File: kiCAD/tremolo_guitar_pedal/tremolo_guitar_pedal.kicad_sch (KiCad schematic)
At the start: 34 parts, among them CN3 NUCLEO-L432KC, CN4 NUCLEO-L432KC, J1 NJ2FD-V, J2 NJ2FD-V, J3 UPduino v3.1, J5 UPduino v3.1, SW1 3PDT Footswitch, U1 NE5532, U2 PCM5102, U3 LD1117DT33CTR

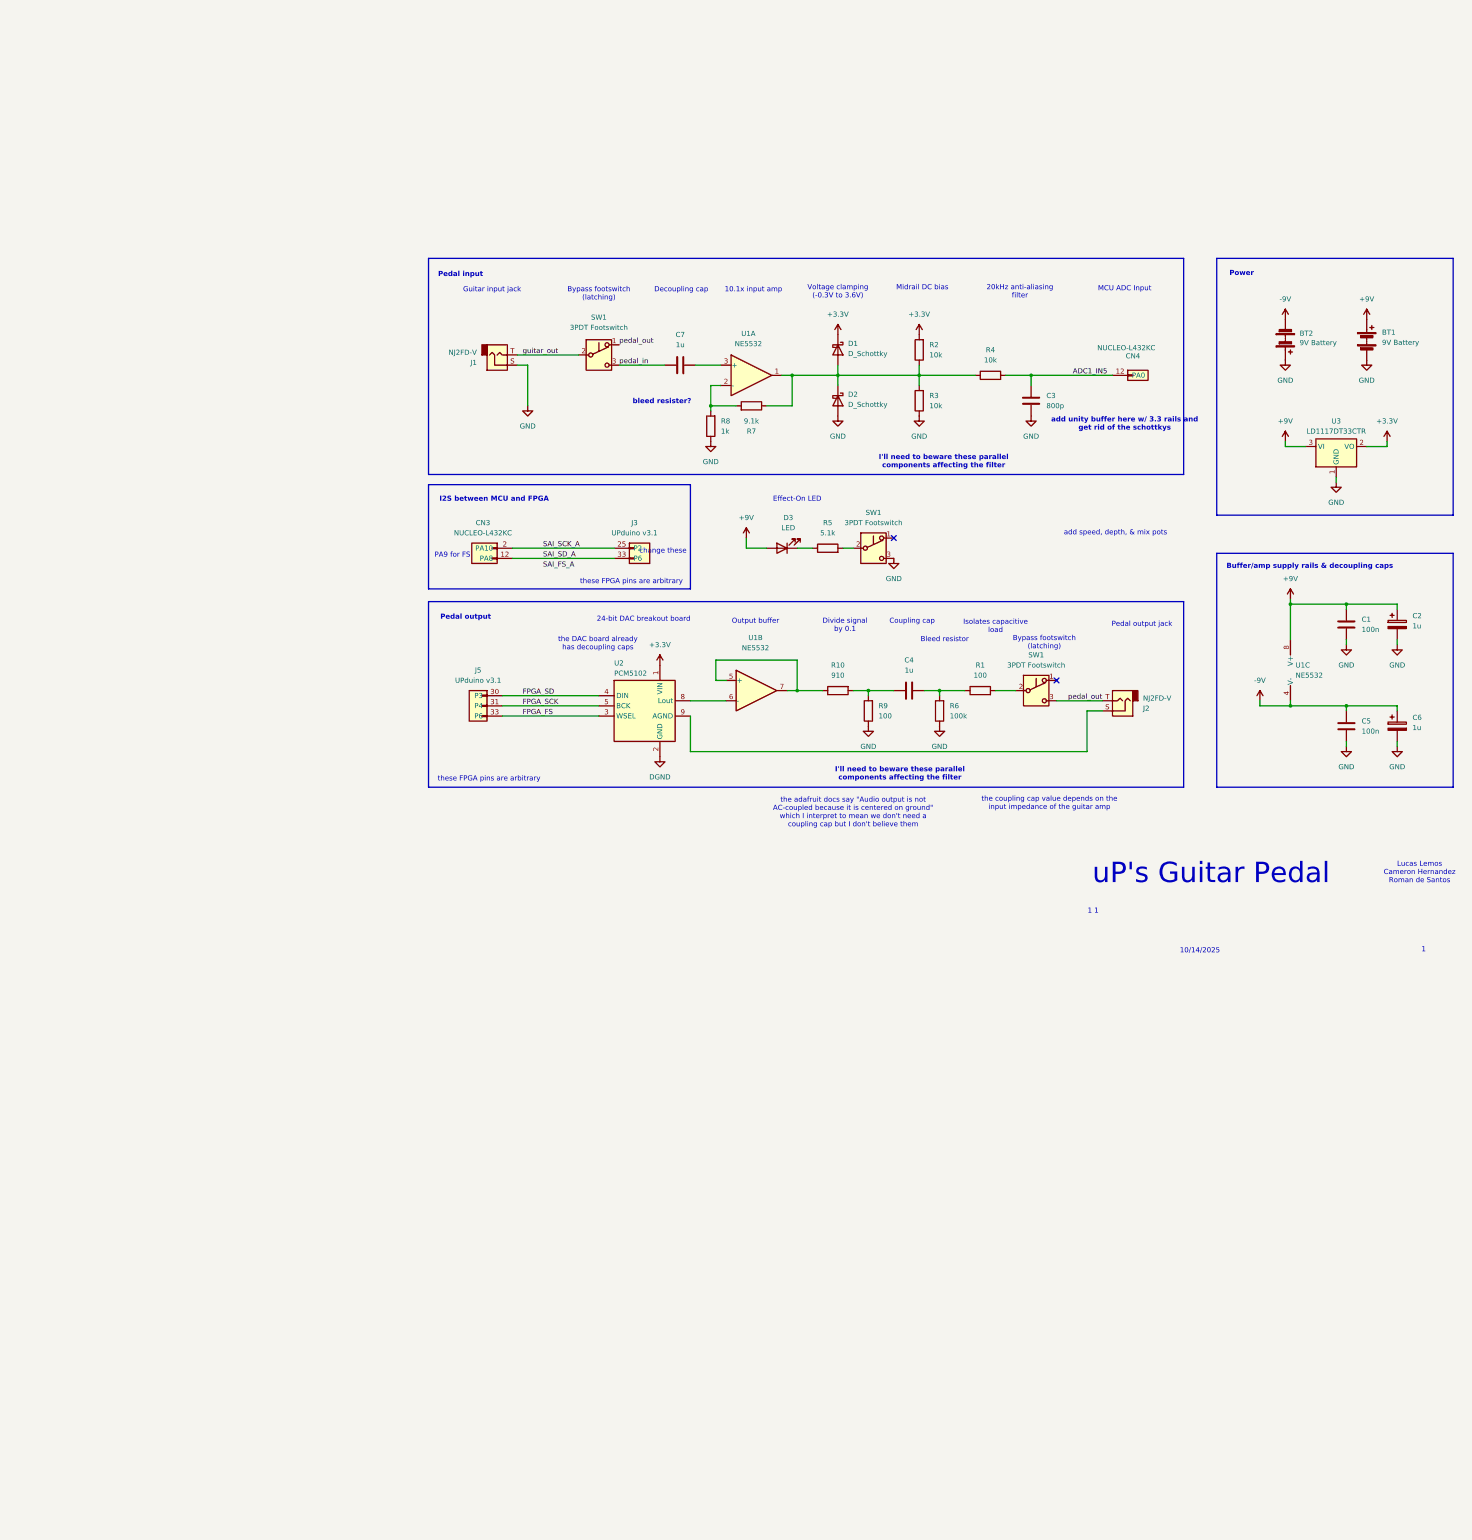
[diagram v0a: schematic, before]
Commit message: first pass at circular buffer
and a few kiCAD edits
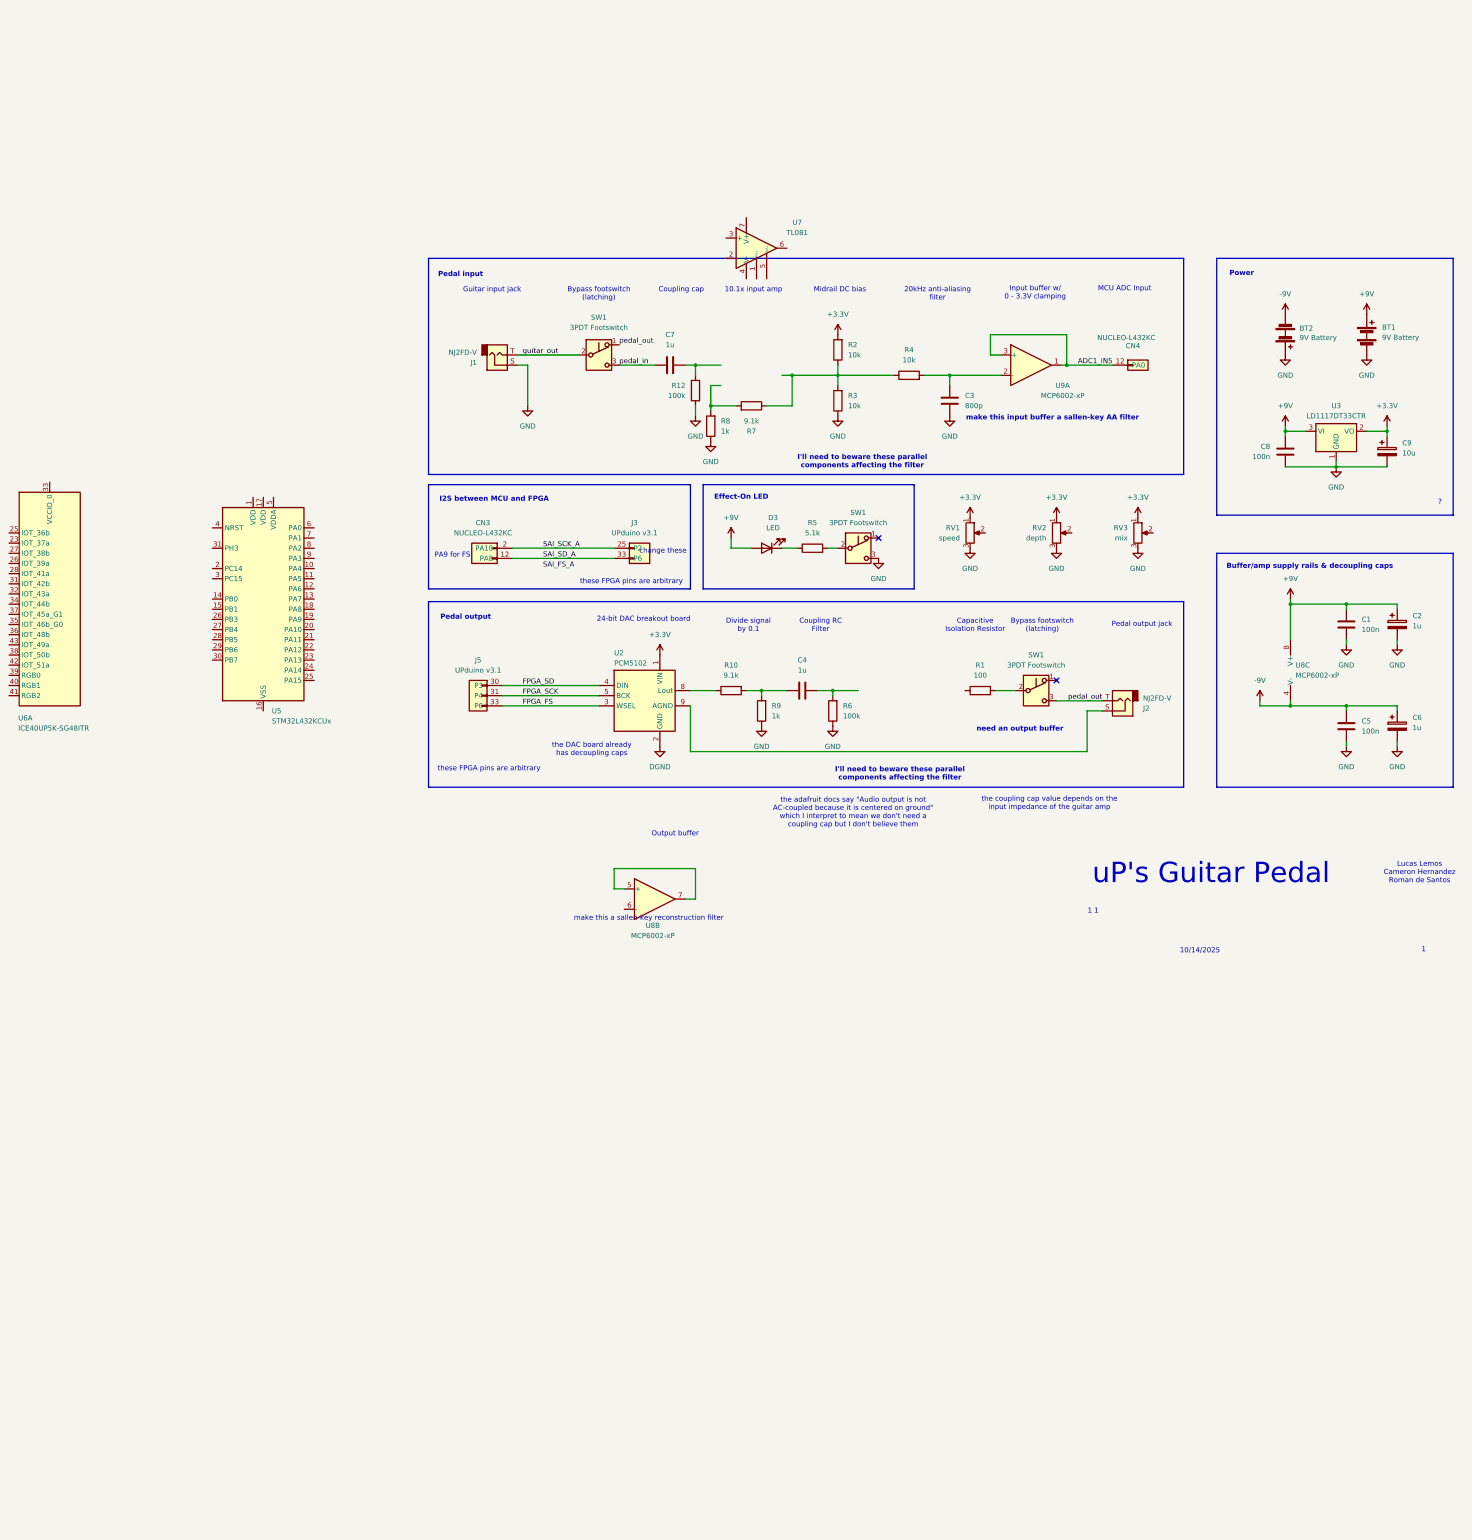
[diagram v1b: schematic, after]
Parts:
- removed D1, D2: D_Schottky, symbol Device:D_Schottky
- removed U1: NE5532, symbol Amplifier_Operational:NE5532
- added C8: 100n, symbol Device:C
- added C9: 10u, symbol Device:C_Polarized
- added R12: 100k, symbol Device:R
- added RV1: speed, symbol Device:R_Potentiometer
- added RV2: depth, symbol Device:R_Potentiometer
- added RV3: mix, symbol Device:R_Potentiometer
- added U5: STM32L432KCUx, Package_DFN_QFN:QFN-32-1EP_5x5mm_P0.5mm_EP3.45x3.45mm, symbol MCU_ST_STM32L4:STM32L432KCUx
- added U6: ICE40UP5K-SG48ITR, Package_DFN_QFN:QFN-48-1EP_7x7mm_P0.5mm_EP5.6x5.6mm, symbol FPGA_Lattice:ICE40UP5K-SG48ITR
- added U7: TL081, symbol Amplifier_Operational:TL081
- added U8, U9: MCP6002-xP, symbol Amplifier_Operational:MCP6002-xP
- R10: value 910 -> 9.1k
- R9: value 100 -> 1k
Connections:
- net +3.3V: now also C9.1, RV1.1, RV2.1, RV3.1
- net +9V: now also C8.1, U8.8 (V+)
- net -9V: now also U8.4 (V-)
- net ADC1_IN5: now also U9.1, U9.3 (+); no longer C3.1, R4.2
- net GND: now also C8.2, C9.2, R12.1, RV1.3, RV2.3, RV3.3
- net at R10.1: now also U2.8 (Lout)
- net at C4.2, R6.2: no longer R1.1
- net at C7.2: now also R12.2
- new net: U8.5 (+), U8.7
- new net: C3.1, R4.2, U9.2 (-)
- new net: U5.16 (VSS), U5.32 (VSS), U5.33 (VSS)
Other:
- note added: "?"
- note added: "Capacitive Isolation Resistor"
- note added: "Coupling RC Filter"
- note added: "Input buffer w/ 0 - 3.3V clamping"
- note added: "make this a sallen-key reconstruction filter"
- note added: "make this input buffer a sallen-key AA filter"
- note added: "need an output buffer"
- note removed: "Bleed resistor"
- note removed: "Decoupling cap"
- note removed: "Isolates capacitive load"
- note removed: "Voltage clamping (-0.3V to 3.6V)"
- note removed: "add speed, depth, & mix pots"
- note removed: "add unity buffer here w/ 3.3 rails and get rid of the schottkys"
- note removed: "bleed resister?"
- moved on the sheet: BT1, BT2, C3, C4, C7, CN4, D3, J5, R10, R2, R3, R4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

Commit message: Analog passthrough works
Assuming an input from the guitar of up to ~280mVpp. I may need to reduce the amplification once I start testing w/ the actual guitar.
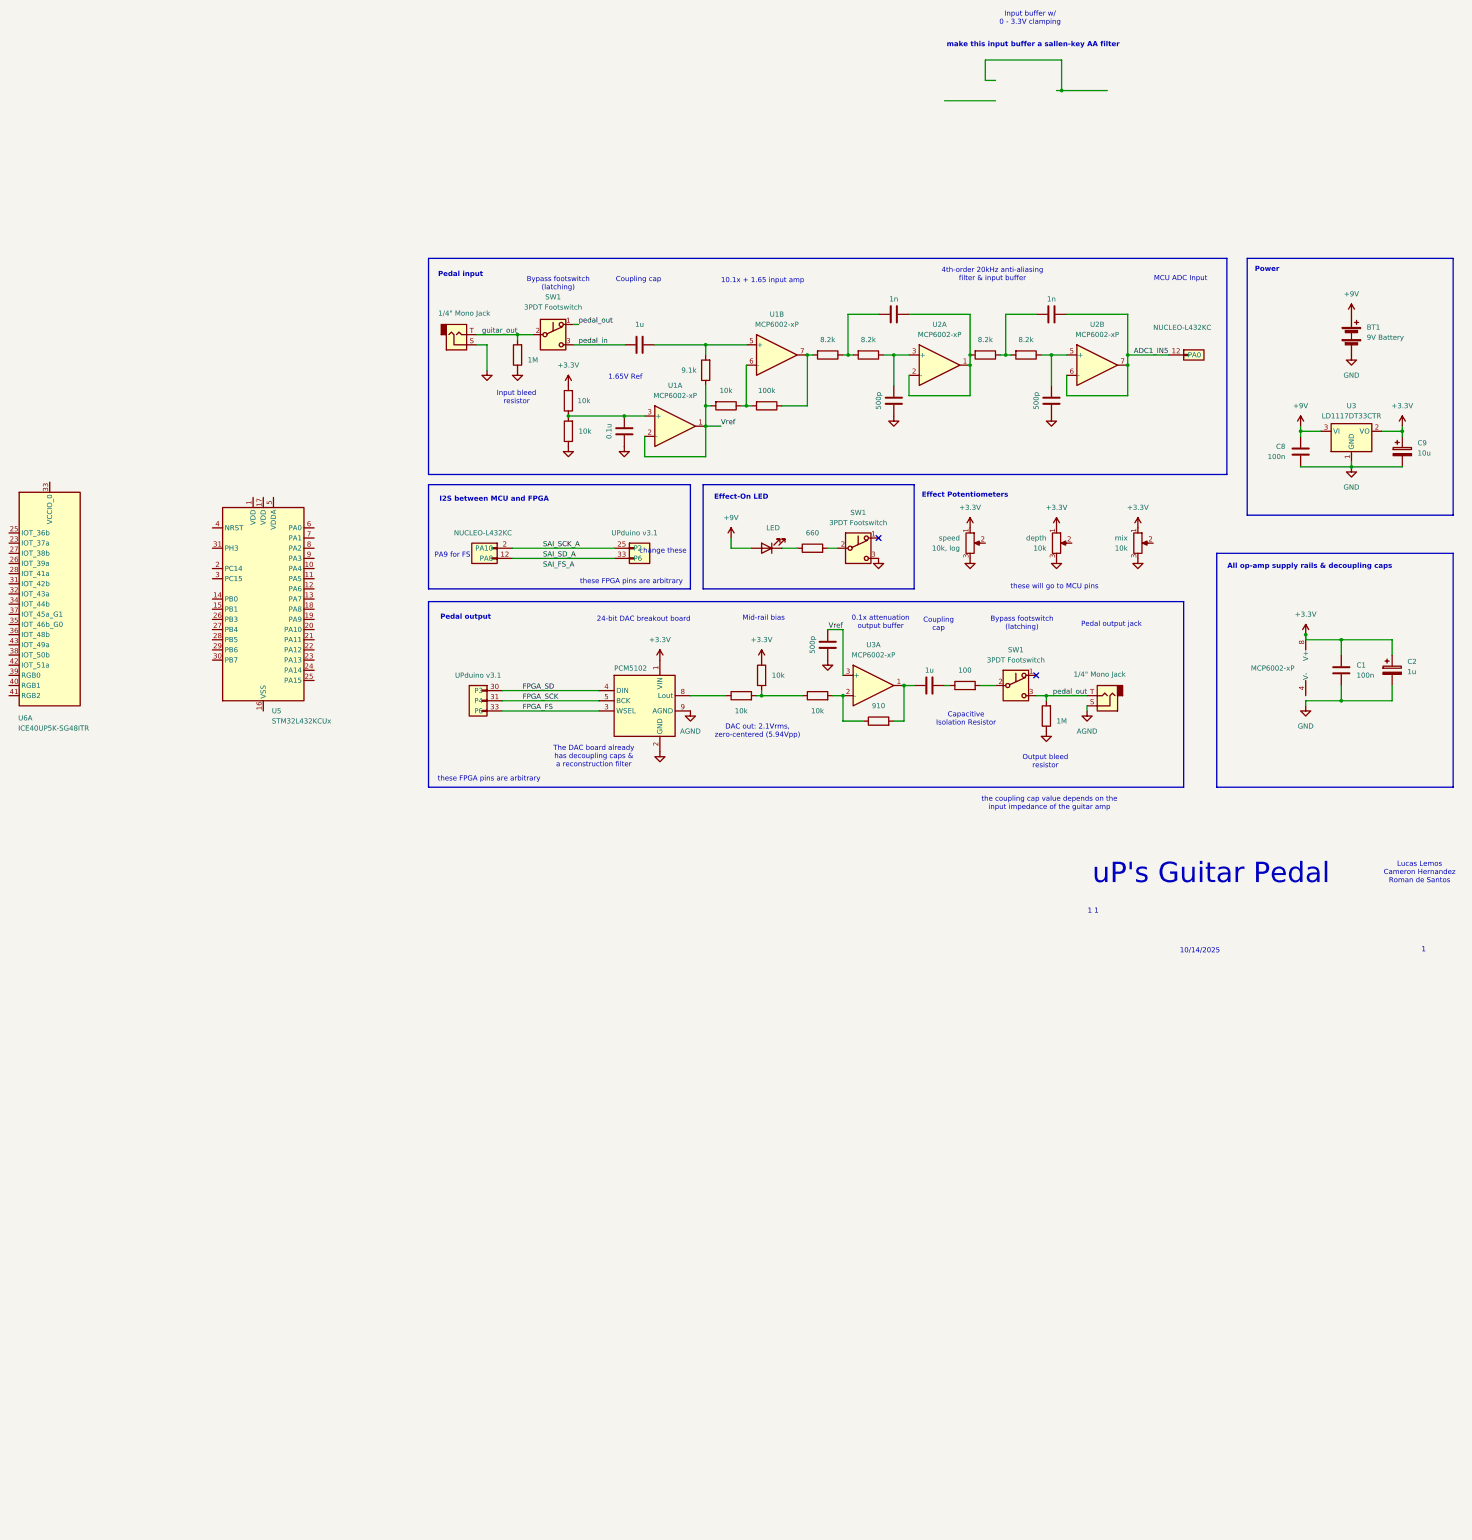
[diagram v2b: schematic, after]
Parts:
- removed BT2: 9V Battery, symbol Device:Battery
- removed C4: 1u, symbol Device:C
- removed C6: 1u, symbol Device:C_Polarized
- removed U7: TL081, symbol Amplifier_Operational:TL081
- removed U8, U9: MCP6002-xP, symbol Amplifier_Operational:MCP6002-xP
- added C10, C11, C12: 500p, symbol Device:C
- added C13: 1u, symbol Device:C
- added C6: 1n, symbol Device:C
- added R11: 100k, symbol Device:R
- added R13, R15: 8.2k, symbol Device:R
- added R14: 1M, symbol Device:R
- added R16: 10k, symbol Device:R
- added R17: 910, symbol Device:R
- added U1, U3: MCP6002-xP, symbol Amplifier_Operational:MCP6002-xP
- added unit 2 of U2
- C3: value 800p -> 1n
- C5: value 100n -> 0.1u
- J1, J2: value NJ2FD-V -> 1/4" Mono Jack
- R10: value 9.1k -> 10k
- R12: value 100k -> 8.2k
- R4: value 10k -> 8.2k
- R5: value 5.1k -> 660
- R6: value 100k -> 1M
- R8, R9: value 1k -> 10k
- depth: renamed from RV2; value depth -> 10k
- mix: renamed from RV3; value mix -> 10k
- speed: renamed from RV1; value speed -> 10k, log
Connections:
- net -9V is gone; now on net GND: C5.1
- net +3.3V: now also C1.1, C2.1, R9.1, U1.8 (V+)
- net +9V: no longer C1.1, C2.1
- net ADC1_IN5: now also C6.2, U2.6 (-), U2.7
- net GND: now also C10.1, C11.1, C12.1, R14.1; no longer C3.2, C5.2, R12.1, R8.1, R9.1
- net guitar_out: now also R6.2
- net pedal_out: now also R14.2
- net at R7.2: now also C7.2, U1.5 (+); no longer R8.2
- net at R10.2, R9.2: now also R16.1
- net at C3.1, R4.2: now also R13.1
- net at R2.1, R3.2: now also C5.2, U1.3 (+); no longer R4.1, R7.1
- net at R1.1: now also C13.2
- net AGND: now reaches J2.S, U2.9 (AGND)
- net at R12.2: now also C3.2, U2.1, U2.2 (-); no longer C7.2
- new net: C10.2, R15.1, U2.5 (+)
- new net: R11.2, R8.1, U1.6 (-)
- new net: R16.2, R17.1, U3.2 (-)
- new net: C13.1, R17.2, U3.1
- new net: C6.1, R12.1, R15.2
- new net: R11.1, R13.2, U1.7
- new net: C11.2, R4.1, U2.3 (+)
- new net Vref: C12.2, R7.1, R8.2, U1.1, U1.2 (-), U3.3 (+)
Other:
- note added: "0.1x attenuation output buffer"
- note added: "1.65V Ref"
- note added: "10.1x + 1.65 input amp"
- note added: "4th-order 20kHz anti-aliasing filter & input buffer"
- note added: "All op-amp supply rails & decoupling caps"
- note added: "DAC out: 2.1Vrms, zero-centered (5.94Vpp)"
- note added: "Effect Potentiometers"
- note added: "Input bleed resistor"
- note added: "Mid-rail bias"
- note added: "Output bleed resistor"
- note added: "The DAC board already has decoupling caps & a reconstruction filter"
- note added: "these will go to MCU pins"
- note removed: "10.1x input amp"
- note removed: "20kHz anti-aliasing filter"
- note removed: "?"
- note removed: "Buffer/amp supply rails & decoupling caps"
- note removed: "Coupling RC Filter"
- note removed: "Divide signal by 0.1"
- note removed: "Guitar input jack"
- note removed: "I'll need to beware these parallel components affecting the filter"
- note removed: "Midrail DC bias"
- note removed: "Output buffer"
- note removed: "make this a sallen-key reconstruction filter"
- note removed: "need an output buffer"
- note removed: "the DAC board already has decoupling caps"
- note removed: "the adafruit docs say "Audio output is not AC-coupled because it is centered on ground" which I interpret to mean we don't need a coupling cap but I don't believe them"
- moved on the sheet: BT1, C1, C2, C8, C9, SW1, U3, depth, mix, speed

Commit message: Some tweaks for simmability
Also updated the .gitignore
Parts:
- removed BT1: 9V Battery, symbol Device:Battery
- added J4: Barrel_Jack, symbol Connector:Barrel_Jack_Switch
- R5: value 660 -> 33
- renumbered SW1 to SW2, SW1 to SW3
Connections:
- net GND: now also SW2.5 (5B), J4.2; no longer SW2.3 (C)
- net pedal_in: now also SW2.4 (A)
- net pedal_out: now also SW3.7 (A); no longer J2.T, R14.2, SW3.3 (C)
- net at R1.2: now also SW3.9 (C); no longer SW3.2 (B)
- net at R5.2: now also SW2.6 (C); no longer SW2.2 (B)
- net +9V renamed +12V
- net +12V: now also J4.1
- new net: J2.T, R14.2, SW3.8 (B)
- no-connect marks 2 -> 1
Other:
- note added: "x3"
- note removed: "Input buffer w/ 0 - 3.3V clamping"
- note removed: "make this input buffer a sallen-key AA filter"
- moved on the sheet: SW2, SW3, U1A

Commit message: Schematic update
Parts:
- added SW4: SW_Depth, symbol Switch:SW_DIP_x04
- added SW5: SW_Speed, symbol Switch:SW_DIP_x04
- added speed1: 10k, log, symbol Device:R_Potentiometer
- R17: value 910 -> 47k
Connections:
- net +12V: no longer D3.2 (A)
- net +3.3V: now also D3.2 (A)
- net ADC1_IN5: now also CN4.9 (PA3); no longer CN4.12 (PA0)
- net GND: now also SW4.1, SW4.2, SW4.3, SW4.4, SW5.1, SW5.2, SW5.3, SW5.4
- net SAI_SCK_A: now also CN3.18 (PA8); no longer CN3.2 (PA10)
- net SAI_SD_A: now also CN3.19 (PA9); no longer CN3.12 (PA8)
- new net P11: SW4.6
- new net P19: SW4.5
- new net P31: SW5.7
- new net P32: SW5.5
- new net P35: SW5.6
- new net P37: SW5.8
- new net P4: SW4.8
- new net P6: SW4.7
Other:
- note added: "Modulation Switches"
- moved on the sheet: U5, U6A, depth, mix, speed
